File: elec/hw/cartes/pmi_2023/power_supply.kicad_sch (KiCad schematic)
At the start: 52 parts, among them J5 254, J8 254, Q3 DMP2008UFG-7, SW8 MSS12C02LS-BB2.0, U28 TLV61070A, U29 TLV61070A, U33 TLV61070A, U34 TLV61070A, U35 LDL1117S33R

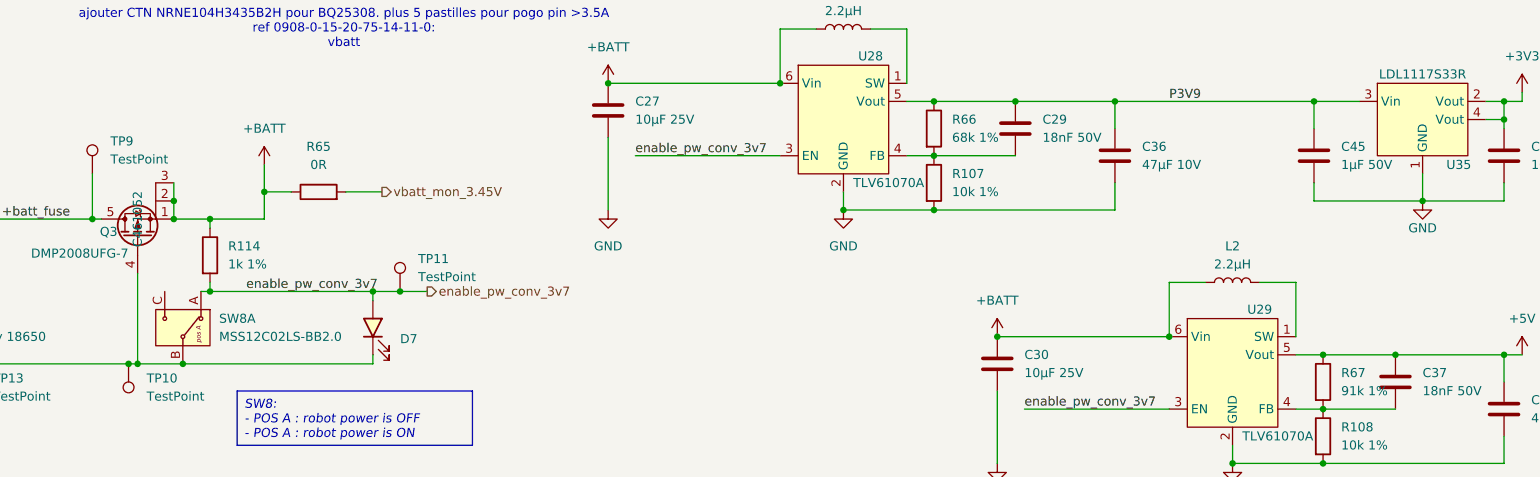
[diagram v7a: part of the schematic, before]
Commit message: bom updated and component selection optimized to decrease bom cost
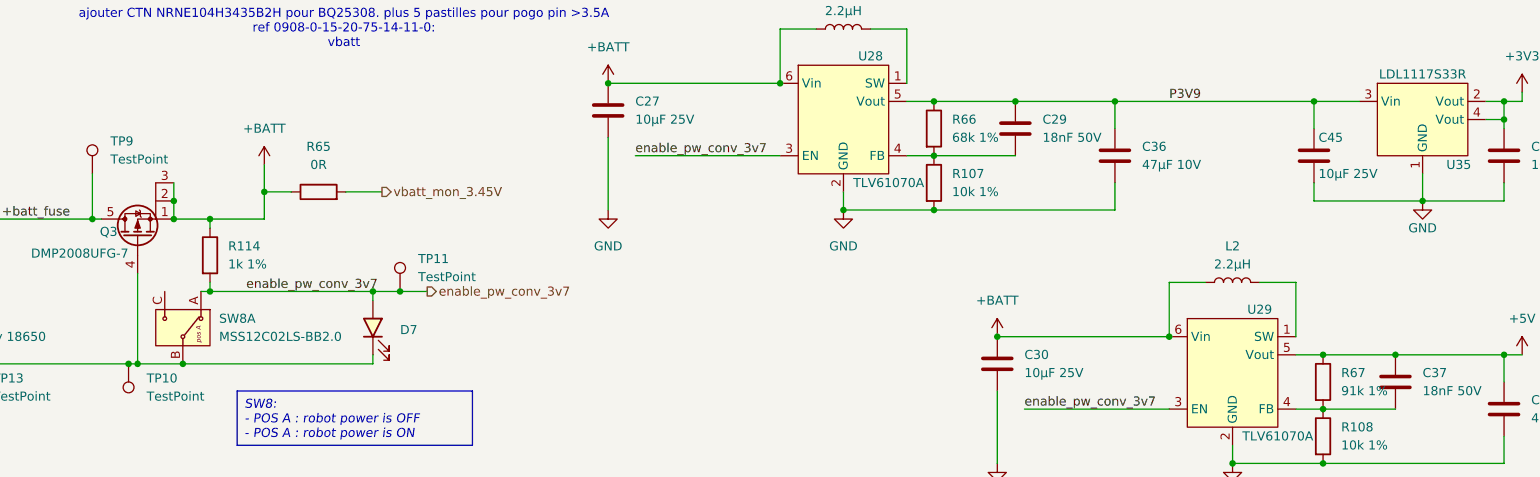
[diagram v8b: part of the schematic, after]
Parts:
- C45: value 1µF 50V -> 10µF 25V; symbol cocotter_capacitors:C_1µF_50V_0805 -> cocotter_capacitors:C_10µF_25V_0805_X5R; JLCPCB Part # C28323 -> C15850; Specification 1µF 50V X7R 0805 -> 10µF 25V X7R 0805
- D7: value white, 0603 -> green, 0603; symbol cocotter_diodes:white_led_0603 -> cocotter_diodes:green_led_0603; DIGIKEY_REF (none) -> 3147-B19Y1UYG-20C000313U1930CT-ND; JLCPCB Part # C2290 -> C22371299; MOUSER_REF (none) -> 710-150060VS55040
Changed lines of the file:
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@@
 	)
 	(symbol
-		(lib_id "cocotter_diodes:white_led_0603")
+		(lib_id "cocotter_diodes:green_led_0603")
 		(at 101.6 62.23 90)
 		(unit 1)
@@
 		(fields_autoplaced yes)
 		(property "Reference" "D7"
-			(at 105.41 63.8174 90)
+			(at 105.41 62.5474 90)
 			(effects
 				(font
@@
 			)
 		)
-		(property "Value" "white, 0603"
+		(property "Value" "green, 0603"
 			(at 104.14 62.23 0)
 			(effects
@@
 			)
 		)
-		(property "Description" "Light emitting diode, white, Vf=[2.6V; 3.1V]"
-			(at 106.172 62.23 0)
+		(property "Description" "Light emitting diode, Green, Vf=[2V; 2.4V]"
+			(at 101.6 62.23 0)
 			(effects
 				(font
@@
 			)
 		)
-		(property "DIGIKEY_REF" ""
+		(property "DIGIKEY_REF" "3147-B19Y1UYG-20C000313U1930CT-ND"
 			(at 101.6 62.23 0)
 			(effects
@@
 			)
 		)
-		(property "MOUSER_REF" ""
+		(property "MOUSER_REF" "710-150060VS55040"
 			(at 101.6 62.23 0)
 			(effects
@@
 			)
 		)
-		(property "JLCPCB Part #" "C2290"
-			(at 101.6 62.23 0)
+		(property "JLCPCB Part #" "C22371299"
+			(at 105.41 65.0874 90)
 			(effects
 				(font
 					(size 1.27 1.27)
 				)
+				(justify right)
 				(hide yes)
 			)
@@
 					(size 1.27 1.27)
 				)
+				(hide yes)
 			)
 		)
@@
 	)
 	(symbol
-		(lib_id "cocotter_capacitors:C_1µF_50V_0805")
+		(lib_id "cocotter_capacitors:C_10µF_25V_0805_X5R")
 		(at 233.68 38.1 0)
 		(unit 1)
@@
 		(dnp no)
 		(property "Reference" "C45"
-			(at 237.49 36.83 0)
+			(at 234.315 35.56 0)
 			(effects
 				(font
@@
 			)
 		)
-		(property "Value" "1µF 50V"
-			(at 237.49 39.37 0)
+		(property "Value" "10µF 25V"
+			(at 234.315 40.64 0)
 			(effects
 				(font
@@
 			)
 		)
-		(property "Description" "Unpolarized capacitor X7R "
+		(property "Description" "Unpolarized capacitor"
 			(at 233.68 38.1 0)
 			(effects
@@
 			)
 		)
-		(property "Specification" "1µF 50V X7R 0805 "
+		(property "Specification" "10µF 25V X7R 0805 "
 			(at 233.68 38.1 0)
 			(effects
@@
 			)
 		)
-		(property "JLCPCB Part #" "C28323"
+		(property "JLCPCB Part #" "C15850"
 			(at 233.68 38.1 0)
 			(effects
